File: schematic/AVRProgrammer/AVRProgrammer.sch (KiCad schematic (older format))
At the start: 22 parts, among them J1 ProMicro_L, J2 ProMicro_R, J3 ProgConn, Q1 BSS138, SW1 Reset, SW2 PowerSelect, U1 LM1117-3.3, U2 MC74VHC1GT125, U3 MC74VHC1GT125, U4 MC74VHC1GT125, U5 MC74VHC1GT125, U6 MC74VHC1GT125, U7 MC74VHC1GT125

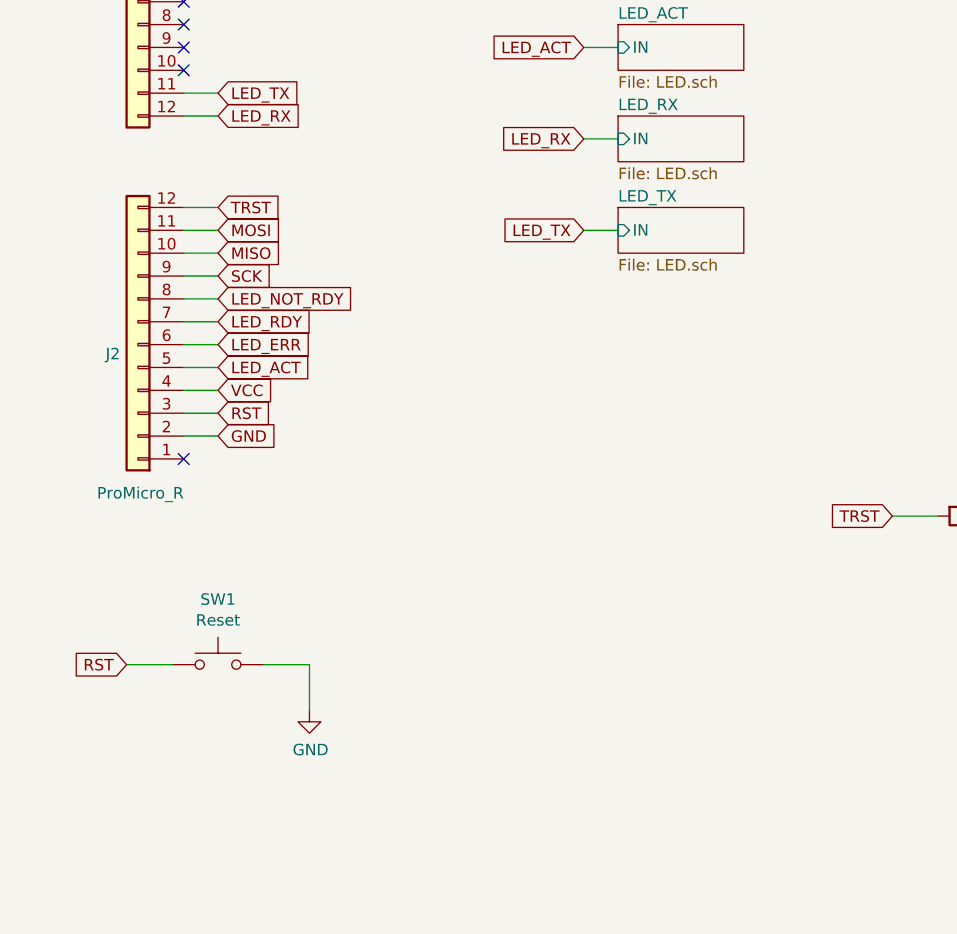
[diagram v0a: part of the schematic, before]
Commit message: 3dmodels for PCB components was added
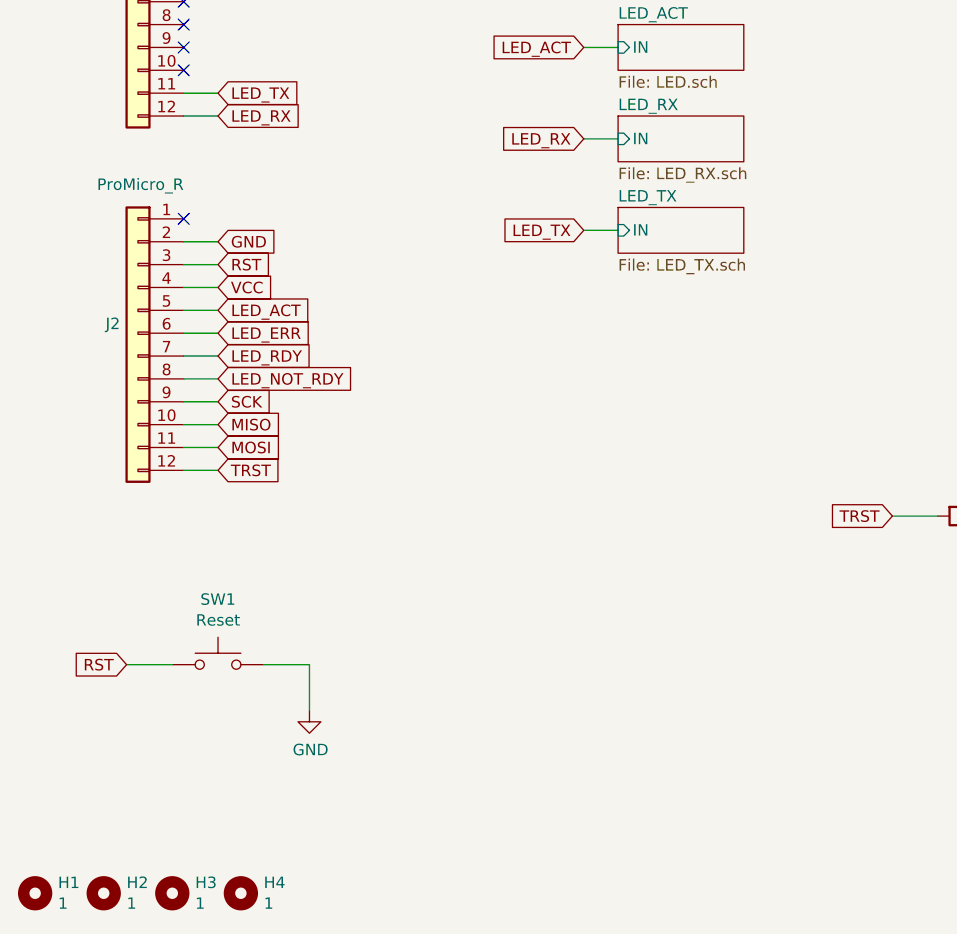
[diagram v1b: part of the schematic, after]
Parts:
- added H1, H2, H3, H4: 1, MountingHole:MountingHole_2.7mm_M2.5, symbol Mechanical:MountingHole
- J1, J2: footprint Connector_PinHeader_2.54mm:PinHeader_1x12_P2.54mm_Vertical -> Connector_PinSocket_2.54mm:PinSocket_1x12_P2.54mm_Vertical
- J3: footprint Connector_PinHeader_2.54mm:PinHeader_2x05_P2.54mm_Horizontal -> Connector_IDC:IDC-Header_2x05_P2.54mm_Horizontal
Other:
- moved on the sheet: J2
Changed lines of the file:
@@
 F 0 "J1" H 1278 3691 50  0000 L CNN
 F 1 "ProMicro_L" H 1000 4300 50  0000 L CNN
-F 2 "Connector_PinHeader_2.54mm:PinHeader_1x12_P2.54mm_Vertical" H 1200 3650 50  0001 C CNN
+F 2 "Connector_PinSocket_2.54mm:PinSocket_1x12_P2.54mm_Vertical" H 1200 3650 50  0001 C CNN
 F 3 "" H 1200 3650 50  0001 C CNN
 	1    1200 3650
@@
 L Connector_Generic:Conn_01x12 J2
 U 1 1 5A59B338
-P 1200 5250
-F 0 "J2" H 1278 5291 50  0000 L CNN
-F 1 "ProMicro_R" H 1000 5900 50  0000 L CNN
-F 2 "Connector_PinHeader_2.54mm:PinHeader_1x12_P2.54mm_Vertical" H 1200 5250 50  0001 C CNN
-F 3 "" H 1200 5250 50  0001 C CNN
-	1    1200 5250
-	-1   0    0    1
+P 1200 5200
+F 0 "J2" H 1278 5241 50  0000 L CNN
+F 1 "ProMicro_R" H 1000 5850 50  0000 L CNN
+F 2 "Connector_PinSocket_2.54mm:PinSocket_1x12_P2.54mm_Vertical" H 1200 5200 50  0001 C CNN
+F 3 "" H 1200 5200 50  0001 C CNN
+	1    1200 5200
+	-1   0    0    -1
 $EndComp
 $Comp
@@
 	1400 4250 1550 4250
 Wire Wire Line
-	1400 4650 1550 4650
-Wire Wire Line
-	1400 4750 1550 4750
-Wire Wire Line
-	1400 4850 1550 4850
-Wire Wire Line
-	1400 4950 1550 4950
-Wire Wire Line
-	1400 5050 1550 5050
-Wire Wire Line
-	1400 5150 1550 5150
-Wire Wire Line
-	1400 5250 1550 5250
-Wire Wire Line
-	1400 5350 1550 5350
-Wire Wire Line
-	1400 5450 1550 5450
-Wire Wire Line
-	1400 5550 1550 5550
-Wire Wire Line
-	1400 5650 1550 5650
+	1400 5800 1550 5800
+Wire Wire Line
+	1400 5700 1550 5700
+Wire Wire Line
+	1400 5600 1550 5600
+Wire Wire Line
+	1400 5500 1550 5500
+Wire Wire Line
+	1400 5400 1550 5400
+Wire Wire Line
+	1400 5300 1550 5300
+Wire Wire Line
+	1400 5200 1550 5200
+Wire Wire Line
+	1400 5100 1550 5100
+Wire Wire Line
+	1400 5000 1550 5000
+Wire Wire Line
+	1400 4900 1550 4900
+Wire Wire Line
+	1400 4800 1550 4800
 Wire Wire Line
 	10550 750  10550 900
@@
 F 0 "J3" H 9800 2465 50  0000 C CNN
 F 1 "ProgConn" H 9800 2374 50  0000 C CNN
-F 2 "Connector_PinHeader_2.54mm:PinHeader_2x05_P2.54mm_Horizontal" H 9800 850 50  0001 C CNN
+F 2 "Connector_IDC:IDC-Header_2x05_P2.54mm_Horizontal" H 9800 850 50  0001 C CNN
 F 3 "" H 9800 850 50  0001 C CNN
 	1    9800 2050
@@
 	7550 5050 7450 5050
 NoConn ~ 10100 2150
-NoConn ~ 1400 5750
+NoConn ~ 1400 4700
 $Comp
 L Switch:SW_Push SW1
@@
 U 5C9FD77F
 F0 "LED_RX" 50
-F1 "LED.sch" 50
+F1 "LED_RX.sch" 50
 F2 "IN" I L 3300 4350 50
 $EndSheet
@@
 U 5CA01110
 F0 "LED_TX" 50
-F1 "LED.sch" 50
+F1 "LED_TX.sch" 50
 F2 "IN" I L 3300 4750 50
 $EndSheet
@@
 Text GLabel 10300 2050 2    50   Input ~ 0
 GND
-Text GLabel 1550 4750 2    50   Input ~ 0
+Text GLabel 1550 5700 2    50   Input ~ 0
 MOSI
 Text GLabel 7500 2600 0    50   Input ~ 0
 SCK
-Text GLabel 1550 4950 2    50   Input ~ 0
+Text GLabel 1550 5500 2    50   Input ~ 0
 SCK
 Text GLabel 8800 2600 2    50   Input ~ 0
@@
 Text GLabel 6350 3800 0    50   Input ~ 0
 MISO
-Text GLabel 1550 4850 2    50   Input ~ 0
+Text GLabel 1550 5600 2    50   Input ~ 0
 MISO
 Text Label 2550 1650 0    50   ~ 0
@@
 Text GLabel 9400 1850 0    50   Input ~ 0
 MISO_P
-Text GLabel 1550 5050 2    50   Input ~ 0
+Text GLabel 1550 5400 2    50   Input ~ 0
 LED_NOT_RDY
-Text GLabel 1550 5150 2    50   Input ~ 0
+Text GLabel 1550 5300 2    50   Input ~ 0
 LED_RDY
-Text GLabel 1550 5250 2    50   Input ~ 0
+Text GLabel 1550 5200 2    50   Input ~ 0
 LED_ERR
-Text GLabel 1550 5350 2    50   Input ~ 0
+Text GLabel 1550 5100 2    50   Input ~ 0
 LED_ACT
-Text GLabel 1550 5450 2    50   Input ~ 0
+Text GLabel 1550 5000 2    50   Input ~ 0
 VCC
-Text GLabel 1550 5550 2    50   Input ~ 0
+Text GLabel 1550 4900 2    50   Input ~ 0
 RST
-Text GLabel 1550 5650 2    50   Input ~ 0
+Text GLabel 1550 4800 2    50   Input ~ 0
 GND
 Text GLabel 1150 6650 0    50   Input ~ 0
@@
 Text GLabel 4500 6000 0    50   Input ~ 0
 TRST
-Text GLabel 1550 4650 2    50   Input ~ 0
+Text GLabel 1550 5800 2    50   Input ~ 0
 TRST
 Text GLabel 1550 3150 2    50   Input ~ 0
@@
 Text GLabel 1550 4150 2    50   Input ~ 0
 LED_TX
+$Comp
+L Mechanical:MountingHole H1
+U 1 1 5CB19C48
+P 750 7650
+F 0 "H1" H 850 7696 50  0000 L CNN
+F 1 "1" H 850 7605 50  0000 L CNN
+F 2 "MountingHole:MountingHole_2.7mm_M2.5" H 750 7650 50  0001 C CNN
+F 3 "~" H 750 7650 50  0001 C CNN
+	1    750  7650
+	1    0    0    -1
+$EndComp
+$Comp
+L Mechanical:MountingHole H2
+U 1 1 5CB1B2C5
+P 1050 7650
+F 0 "H2" H 1150 7696 50  0000 L CNN
+F 1 "1" H 1150 7605 50  0000 L CNN
+F 2 "MountingHole:MountingHole_2.7mm_M2.5" H 1050 7650 50  0001 C CNN
+F 3 "~" H 1050 7650 50  0001 C CNN
+	1    1050 7650
+	1    0    0    -1
+$EndComp
+$Comp
+L Mechanical:MountingHole H3
+U 1 1 5CB1B425
+P 1350 7650
+F 0 "H3" H 1450 7696 50  0000 L CNN
+F 1 "1" H 1450 7605 50  0000 L CNN
+F 2 "MountingHole:MountingHole_2.7mm_M2.5" H 1350 7650 50  0001 C CNN
+F 3 "~" H 1350 7650 50  0001 C CNN
+	1    1350 7650
+	1    0    0    -1
+$EndComp
+$Comp
+L Mechanical:MountingHole H4
+U 1 1 5CB1B5E8
+P 1650 7650
+F 0 "H4" H 1750 7696 50  0000 L CNN
+F 1 "1" H 1750 7605 50  0000 L CNN
+F 2 "MountingHole:MountingHole_2.7mm_M2.5" H 1650 7650 50  0001 C CNN
+F 3 "~" H 1650 7650 50  0001 C CNN
+	1    1650 7650
+	1    0    0    -1
+$EndComp
 $EndSCHEMATC
